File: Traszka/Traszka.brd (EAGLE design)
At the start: 30.1 x 58.4 mm, 18 parts, among them IC1 MEGA8-P, IC2 7818TV, T1 BC547, X3 CRYSTALS-NOGND-HC49

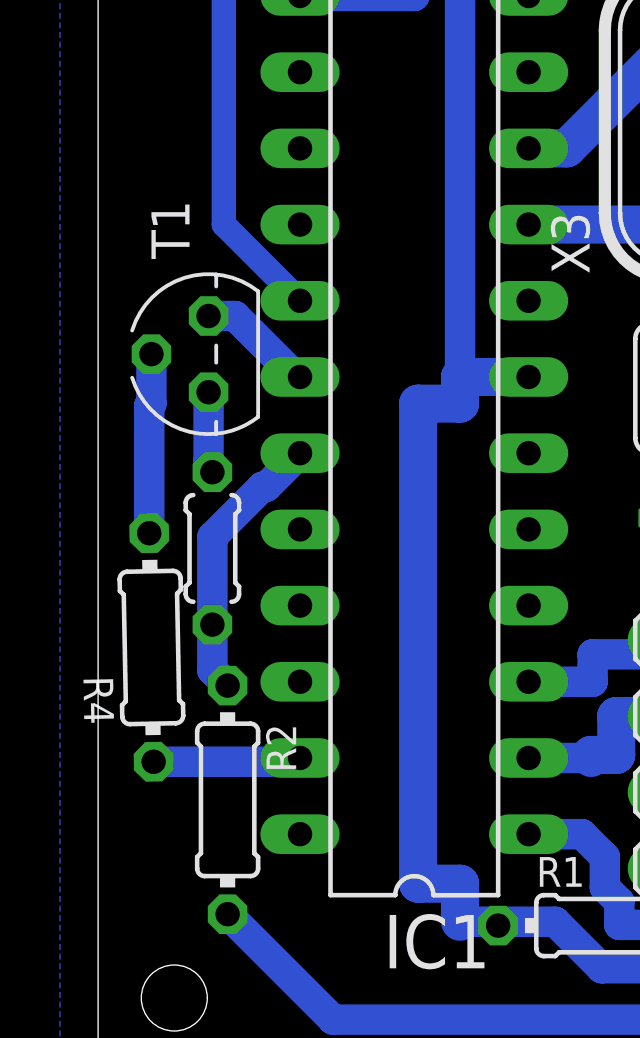
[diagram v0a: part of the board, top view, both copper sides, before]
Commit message: fixing .sch and .brd checking battery
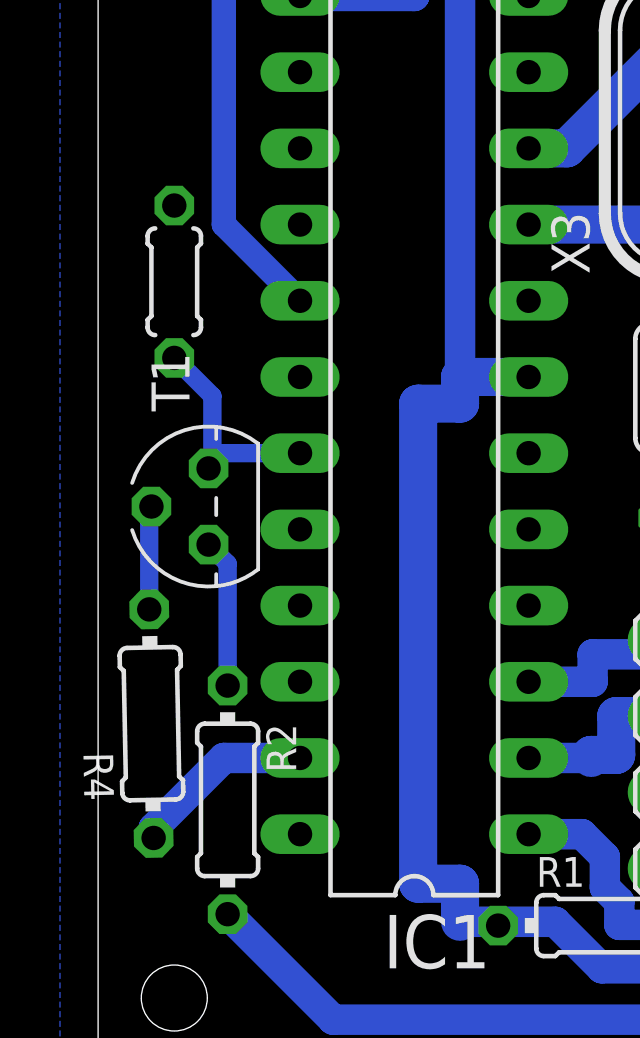
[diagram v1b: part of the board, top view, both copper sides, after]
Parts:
- moved R3 8.98 mm to (2.54, 26.4)
- moved T1 5.08 mm to (3.68, 18.9)
- moved R4 2.54 mm to (1.78, 11.7)
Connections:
- removed net N$4 (its old number): R3.1, T1.3
- new net N$3: R2.1, T1.3
- net GND: now also R3.1; no longer T1.1
- net VCCREF: now also T1.1; no longer R2.1
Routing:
- net N$3: track 0.00 -> 4.96 mm
- net GND: track 3.89 -> 0.13 mm
- net N$4 (its old number): track 2.69 -> 0.00 mm
- net N$4: track 6.00 -> 3.46 mm
- net VCCREF: track 9.24 -> 7.34 mm
- net CHECK_VIN: track 4.93 -> 6.18 mm
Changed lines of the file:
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@@
 <attribute name="VALUE" x="3.8354" y="10.7696" size="0.9906" layer="27" ratio="10" rot="R270"/>
 </element>
-<element name="R3" library="rcl" library_urn="urn:adsk.eagle:library:334" package="0204/5" package3d_urn="urn:adsk.eagle:package:23488/1" value="" x="3.81" y="17.526" smashed="yes" rot="R270">
-<attribute name="POPULARITY" value="35" x="3.81" y="17.526" size="1.778" layer="27" rot="R270" display="off"/>
-<attribute name="SPICEPREFIX" value="R" x="3.81" y="17.526" size="1.778" layer="27" rot="R270" display="off"/>
-<attribute name="VALUE" x="3.3274" y="19.1516" size="0.9906" layer="27" ratio="10" rot="R270"/>
+<element name="R3" library="rcl" library_urn="urn:adsk.eagle:library:334" package="0204/5" package3d_urn="urn:adsk.eagle:package:23488/1" value="" x="2.54" y="26.416" smashed="yes" rot="R270">
+<attribute name="POPULARITY" value="35" x="2.54" y="26.416" size="1.778" layer="27" rot="R270" display="off"/>
+<attribute name="SPICEPREFIX" value="R" x="2.54" y="26.416" size="1.778" layer="27" rot="R270" display="off"/>
+<attribute name="VALUE" x="2.0574" y="28.0416" size="0.9906" layer="27" ratio="10" rot="R270"/>
 </element>
 <element name="C5" library="rcl" library_urn="urn:adsk.eagle:library:334" package="C050-024X044" package3d_urn="urn:adsk.eagle:package:23643/1" value="" x="3.81" y="40.64" smashed="yes" rot="R90">
@@
 <attribute name="VALUE" x="6.477" y="38.481" size="1.27" layer="27" ratio="10" rot="R90"/>
 </element>
-<element name="T1" library="transistor" library_urn="urn:adsk.eagle:library:402" package="TO92" package3d_urn="urn:adsk.eagle:package:28523/2" value="BC547" x="3.683" y="24.003" smashed="yes" rot="R90">
-<attribute name="NAME" x="3.048" y="27.178" size="1.27" layer="25" ratio="10" rot="R90"/>
-<attribute name="POPULARITY" value="43" x="3.683" y="24.003" size="1.778" layer="27" rot="R90" display="off"/>
-<attribute name="VALUE" x="4.953" y="27.178" size="1.27" layer="27" ratio="10" rot="R90"/>
-</element>
-<element name="R4" library="rcl" library_urn="urn:adsk.eagle:library:334" package="0204/7" package3d_urn="urn:adsk.eagle:package:23498/2" value="" x="1.778" y="14.224" smashed="yes" rot="R91.1">
-<attribute name="NAME" x="0.531603125" y="11.65960625" size="0.9906" layer="25" ratio="10" rot="R91.1"/>
-<attribute name="POPULARITY" value="79" x="1.778" y="14.224" size="1.778" layer="27" rot="R91.1" display="off"/>
-<attribute name="SPICEPREFIX" value="R" x="1.778" y="14.224" size="1.778" layer="27" rot="R91.1" display="off"/>
-<attribute name="VALUE" x="2.291721875" y="12.607965625" size="0.9906" layer="27" ratio="10" rot="R91.1"/>
+<element name="R4" library="rcl" library_urn="urn:adsk.eagle:library:334" package="0204/7" package3d_urn="urn:adsk.eagle:package:23498/2" value="" x="1.778" y="11.684" smashed="yes" rot="R91.1">
+<attribute name="NAME" x="0.531603125" y="9.11960625" size="0.9906" layer="25" ratio="10" rot="R91.1"/>
+<attribute name="POPULARITY" value="79" x="1.778" y="11.684" size="1.778" layer="27" rot="R91.1" display="off"/>
+<attribute name="SPICEPREFIX" value="R" x="1.778" y="11.684" size="1.778" layer="27" rot="R91.1" display="off"/>
+<attribute name="VALUE" x="2.291721875" y="10.067965625" size="0.9906" layer="27" ratio="10" rot="R91.1"/>
+</element>
+<element name="T1" library="transistor" library_urn="urn:adsk.eagle:library:402" package="TO92" package3d_urn="urn:adsk.eagle:package:28523/2" value="BC547" x="3.683" y="18.923" smashed="yes" rot="R90">
+<attribute name="NAME" x="3.048" y="22.098" size="1.27" layer="25" ratio="10" rot="R90"/>
+<attribute name="POPULARITY" value="43" x="3.683" y="18.923" size="1.778" layer="27" rot="R90" display="off"/>
+<attribute name="VALUE" x="4.953" y="22.098" size="1.27" layer="27" ratio="10" rot="R90"/>
 </element>
 </elements>
@@
 <contactref element="IC1" pad="22"/>
 <contactref element="C5" pad="2"/>
-<contactref element="T1" pad="1"/>
 <wire x1="6.731" y1="23.241" x2="6.59901875" y2="23.241" width="1.016" layer="16"/>
-<wire x1="6.59901875" y1="23.241" x2="4.56701875" y2="25.273" width="1.016" layer="16"/>
-<wire x1="4.56701875" y1="25.273" x2="3.683" y2="25.273" width="1.016" layer="16"/>
+<contactref element="R3" pad="1"/>
+<wire x1="6.59901875" y1="23.241" x2="2.54" y2="28.956" width="0" layer="19" extent="16-16"/>
 </signal>
 <signal name="AVCC">
@@
 </signal>
 <signal name="VCCREF">
-<contactref element="R2" pad="1"/>
+<contactref element="IC1" pad="23"/>
 <contactref element="R3" pad="2"/>
-<contactref element="IC1" pad="23"/>
-<wire x1="3.81" y1="14.986" x2="3.81" y2="13.462" width="1.016" layer="16"/>
-<wire x1="3.81" y1="13.462" x2="4.318" y2="12.954" width="1.016" layer="16"/>
-<wire x1="6.731" y1="20.701" x2="5.6134" y2="19.5834" width="1.016" layer="16"/>
-<wire x1="5.6134" y1="19.5834" x2="5.48141875" y2="19.5834" width="1.016" layer="16"/>
-<wire x1="5.48141875" y1="19.5834" x2="3.81" y2="17.91198125" width="1.016" layer="16"/>
-<wire x1="3.81" y1="17.91198125" x2="3.81" y2="14.986" width="1.016" layer="16"/>
+<contactref element="T1" pad="1"/>
+<wire x1="3.683" y1="20.193" x2="3.81" y2="20.32" width="0.6096" layer="16"/>
+<wire x1="3.81" y1="20.32" x2="4.191" y2="20.701" width="0.6096" layer="16"/>
+<wire x1="4.191" y1="20.701" x2="6.731" y2="20.701" width="0.6096" layer="16"/>
+<wire x1="2.54" y1="23.876" x2="3.81" y2="22.606" width="0.6096" layer="16"/>
+<wire x1="3.81" y1="22.606" x2="3.81" y2="20.32" width="0.6096" layer="16"/>
 </signal>
 <signal name="N$2">
@@
 <wire x1="4.191" y1="37.719" x2="3.81" y2="38.1" width="0.8128" layer="16"/>
 </signal>
-<signal name="N$4">
-<contactref element="R3" pad="1"/>
-<contactref element="T1" pad="3"/>
-<wire x1="3.683" y1="22.733" x2="3.683" y2="20.447" width="1.016" layer="16"/>
-<wire x1="3.683" y1="20.447" x2="3.81" y2="20.066" width="1.016" layer="16"/>
-</signal>
 <signal name="CHECK_VIN">
 <contactref element="R4" pad="1"/>
 <contactref element="IC1" pad="27"/>
-<wire x1="6.731" y1="10.541" x2="6.6047" y2="10.4147" width="1.016" layer="16"/>
-<wire x1="6.6047" y1="10.4147" x2="1.851140625" y2="10.4147" width="1.016" layer="16"/>
+<wire x1="6.731" y1="10.541" x2="4.191" y2="10.541" width="1.016" layer="16"/>
+<wire x1="4.191" y1="10.541" x2="1.851140625" y2="8.201140625" width="1.016" layer="16"/>
+<wire x1="1.851140625" y1="8.201140625" x2="1.851140625" y2="7.8747" width="1.016" layer="16"/>
+</signal>
+<signal name="N$4">
+<contactref element="R4" pad="2"/>
+<contactref element="T1" pad="2"/>
+<wire x1="1.70485625" y1="15.493296875" x2="1.70485625" y2="18.84985625" width="0.6096" layer="16"/>
+<wire x1="1.70485625" y1="18.84985625" x2="1.778" y2="18.923" width="0.6096" layer="16"/>
 </signal>
 <signal name="N$3">
-<contactref element="T1" pad="2"/>
-<contactref element="R4" pad="2"/>
-<wire x1="1.70485625" y1="22.27885625" x2="1.70485625" y2="18.033296875" width="1.016" layer="16"/>
-<wire x1="1.778" y1="24.003" x2="1.778" y2="22.352" width="1.016" layer="16"/>
-<wire x1="1.778" y1="22.352" x2="1.70485625" y2="22.27885625" width="1.016" layer="16"/>
+<contactref element="T1" pad="3"/>
+<contactref element="R2" pad="1"/>
+<wire x1="3.683" y1="17.653" x2="4.318" y2="17.018" width="0.6096" layer="16"/>
+<wire x1="4.318" y1="17.018" x2="4.318" y2="12.954" width="0.6096" layer="16"/>
 </signal>
 </signals>
